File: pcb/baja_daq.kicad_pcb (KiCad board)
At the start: 4 copper layers, 65 x 65 mm, 57 parts, among them J1 Micro_SD_Card, J3 Conn_01x03, J4 Conn_01x03, J7 Conn_01x02, U1 STM32F405RGTx, U2 TJA1051T, U4 L7805, U5 AMS1117-3.3, Y1 8MHz

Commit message: second
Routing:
- net GND: track 45.2 -> 48.6 mm, vias 74 -> 73
- net +5V_ANA: vias 1 -> 2

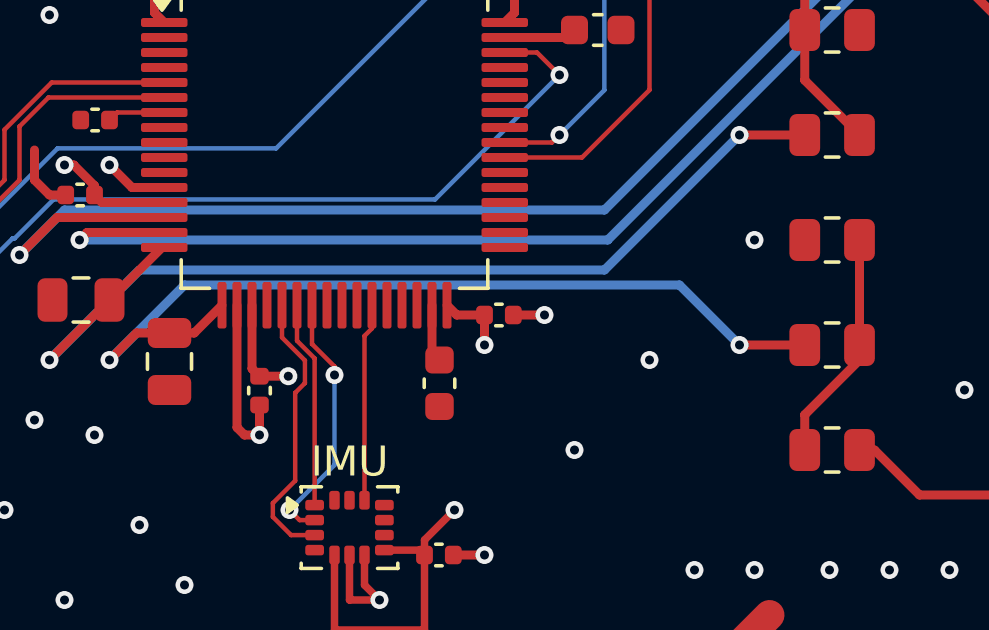
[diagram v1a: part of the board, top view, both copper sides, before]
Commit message: modified layer3 (power split)
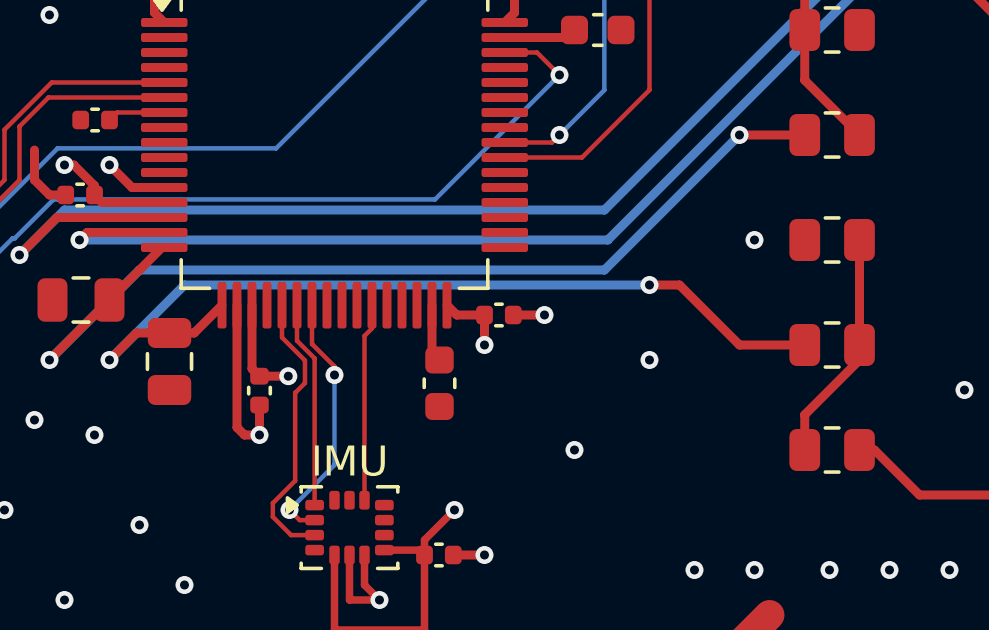
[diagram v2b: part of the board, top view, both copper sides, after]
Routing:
- net +12V_BATT: track 85.5 -> 68.9 mm
- net +5V_ANA: track 265.7 -> 273.2 mm
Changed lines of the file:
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@@
-	)
-	(segment
-		(start 120.603087 108.5)
-		(end 99.603087 129.5)
-		(width 0.6)
-		(layer "In2.Cu")
-		(net "+5V_ANA")
-	)
-	(segment
-		(start 99.603087 129.5)
-		(end 98.5 129.5)
-		(width 0.6)
-		(layer "In2.Cu")
-		(net "+5V_ANA")
 	)
 	(segment
@@
 	)
 	(segment
-		(start 137.5 93)
-		(end 122 108.5)
+		(start 136 94.5)
+		(end 136 110)
+		(width 0.6)
+		(layer "In2.Cu")
+		(net "+5V_ANA")
+	)
+	(segment
+		(start 136 110)
+		(end 116.5 129.5)
 		(width 0.6)
 		(layer "In2.Cu")
@@
 	)
 	(segment
+		(start 137.5 93)
+		(end 136 94.5)
+		(width 0.6)
+		(layer "In2.Cu")
+		(net "+5V_ANA")
+	)
+	(segment
 		(start 134 140.5)
 		(end 136 138.5)
@@
 	)
 	(segment
+		(start 116.5 129.5)
+		(end 100 129.5)
+		(width 0.6)
+		(layer "In2.Cu")
+		(net "+5V_ANA")
+	)
+	(segment
 		(start 140.5 127)
 		(end 140.5 135.5)
@@
 	)
 	(segment
-		(start 122 108.5)
-		(end 120.603087 108.5)
-		(width 0.6)
-		(layer "In2.Cu")
-		(net "+5V_ANA")
-	)
-	(segment
 		(start 133.5 142.5)
 		(end 105.5 142.5)
@@
 	)
 	(segment
+		(start 119.5 130.5)
+		(end 119.5 131.5)
+		(width 0.6)
+		(layer "In2.Cu")
+		(net "+12V_BATT")
+	)
+	(segment
+		(start 118 130.5)
+		(end 118 131.5)
+		(width 0.6)
+		(layer "In2.Cu")
+		(net "+12V_BATT")
+	)
+	(segment
+		(start 140.5 108)
+		(end 118 130.5)
+		(width 0.6)
+		(layer "In2.Cu")
+		(net "+12V_BATT")
+	)
+	(segment
 		(start 140.5 102)
-		(end 132.896913 102)
+		(end 140.5 108)
 		(width 0.6)
 		(layer "In2.Cu")
@@
 	)
 	(segment
-		(start 110.5 124.396913)
-		(end 110.5 131.5)
+		(start 140.5 111)
+		(end 139 111)
 		(width 0.6)
 		(layer "In2.Cu")
@@
 	)
 	(segment
-		(start 140.5 111)
-		(end 128.896913 111)
-		(width 0.6)
-		(layer "In2.Cu")
-		(net "+12V_BATT")
-	)
-	(segment
-		(start 112 127.896913)
-		(end 112 131.5)
-		(width 0.6)
-		(layer "In2.Cu")
-		(net "+12V_BATT")
-	)
-	(segment
-		(start 128.896913 111)
-		(end 112 127.896913)
-		(width 0.6)
-		(layer "In2.Cu")
-		(net "+12V_BATT")
-	)
-	(segment
-		(start 132.896913 102)
-		(end 110.5 124.396913)
+		(start 139 111)
+		(end 119.5 130.5)
 		(width 0.6)
 		(layer "In2.Cu")
@@
 	)
 	(segment
-		(start 129.175 118.5)
+		(start 125 116.5)
 		(end 127 118.5)
 		(width 0.3)
@@
 	)
 	(segment
+		(start 124 116.5)
+		(end 125 116.5)
+		(width 0.3)
+		(layer "F.Cu")
+		(net "SUSP_RR_FLT")
+	)
+	(segment
 		(start 108 118.1)
 		(end 106.9 118.1)
@@
 		(net "SUSP_RR_FLT")
 	)
-	(via
-		(at 127 118.5)
-		(size 0.6)
-		(drill 0.3)
-		(layers "F.Cu" "B.Cu")
+	(segment
+		(start 127 118.5)
+		(end 129.175 118.5)
+		(width 0.3)
+		(layer "F.Cu")
 		(net "SUSP_RR_FLT")
 	)
 	(via
+		(at 124 116.5)
+		(size 0.6)
+		(drill 0.3)
+		(layers "F.Cu" "B.Cu")
+		(net "SUSP_RR_FLT")
+	)
+	(via
 		(at 106 119)
 		(size 0.6)
 		(drill 0.3)
 		(layers "F.Cu" "B.Cu")
-		(net "SUSP_RR_FLT")
-	)
-	(segment
-		(start 127 118.5)
-		(end 125 116.5)
-		(width 0.3)
-		(layer "B.Cu")
 		(net "SUSP_RR_FLT")
 	)
@@
 	)
 	(segment
-		(start 125 116.5)
+		(start 124 116.5)
 		(end 108.5 116.5)
 		(width 0.3)
